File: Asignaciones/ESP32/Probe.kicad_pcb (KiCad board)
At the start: 4 copper layers, 34 x 46.5 mm, 36 parts, among them J2 USB_B_Micro, J4 Conn_01x17, J5 Conn_01x17, Q1 2SC4213, Q2 2SC4213, U1 esp32-devkitM-1, U2 CP2102N-Axx-xQFN28, U4 LM1117MP-3.3

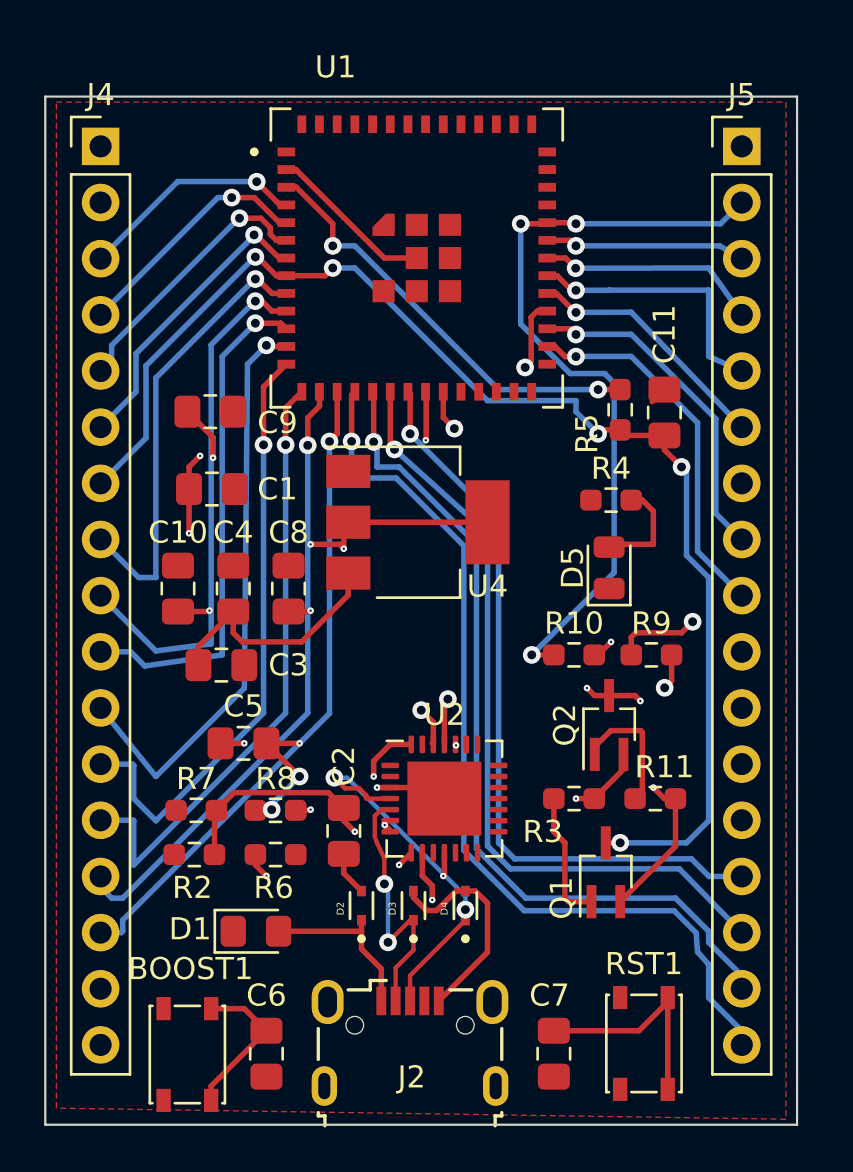
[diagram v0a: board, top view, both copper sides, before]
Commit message: Nuevas asignaciones y cambios
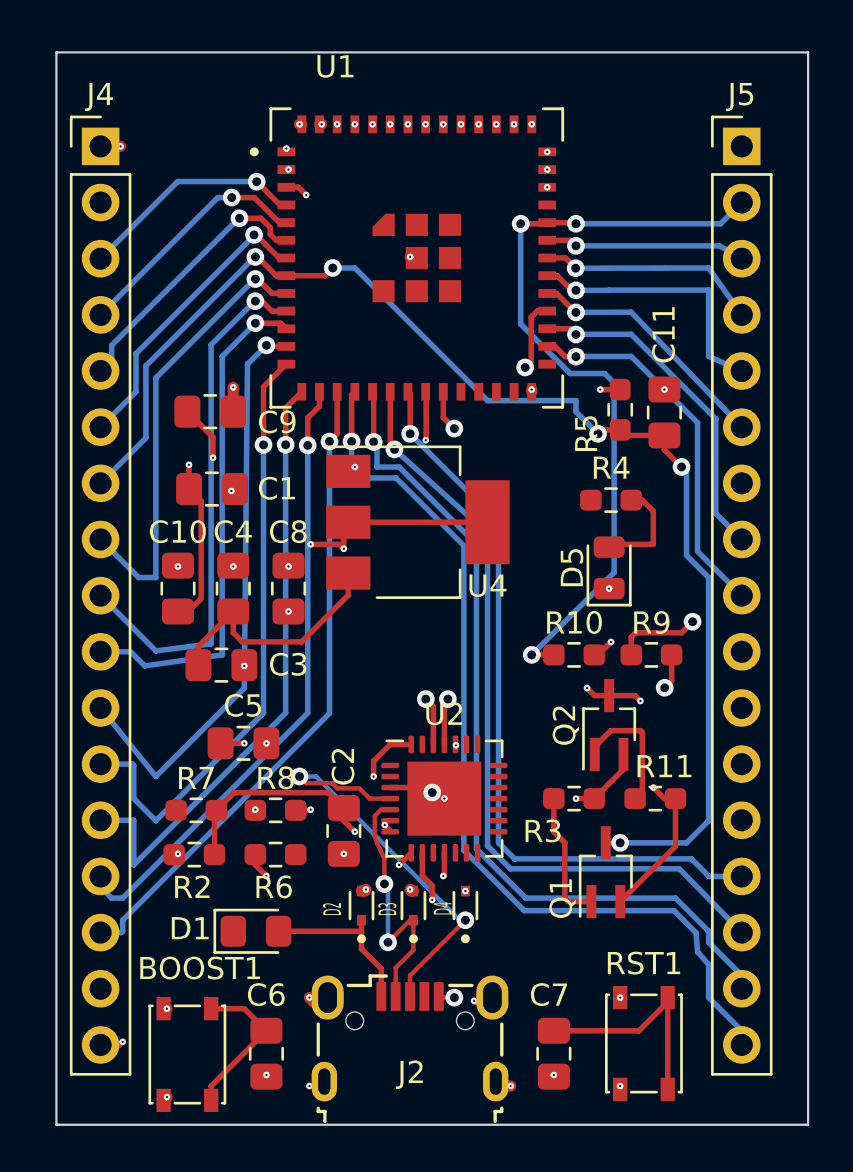
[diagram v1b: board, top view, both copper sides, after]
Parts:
- moved J2 0.20 mm to (198.0, 110.3)
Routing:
- net GND: track 35.0 -> 13.2 mm, vias 4 -> 52
- net Net-(U1-3V3): track 40.5 -> 46.9 mm, vias 5 -> 3
- net /USB_DP: track 16.9 -> 19.4 mm
- net /GPIO23: track 16.3 -> 15.2 mm
- net Net-(U2-TXD): track 17.0 -> 17.7 mm
- net /GPIO12: track 42.3 -> 41.6 mm
- net /GPIO13: track 39.1 -> 38.5 mm
- net Net-(U4-VO): track 22.2 -> 21.6 mm
- net /GPIO4: track 23.9 -> 23.4 mm
- added copper zone on In2.Cu, net GND
- removed copper zone on F.Cu, net GND
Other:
- board size 34 x 46.5 mm -> 34 x 48.5 mm
